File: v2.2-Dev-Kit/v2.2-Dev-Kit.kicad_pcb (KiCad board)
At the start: 2 copper layers, 42 x 59 mm, 30 parts, among them SW1 Up, SW2 Down, SW3 Left, SW4 Right, U1 WeMos D1 Mini

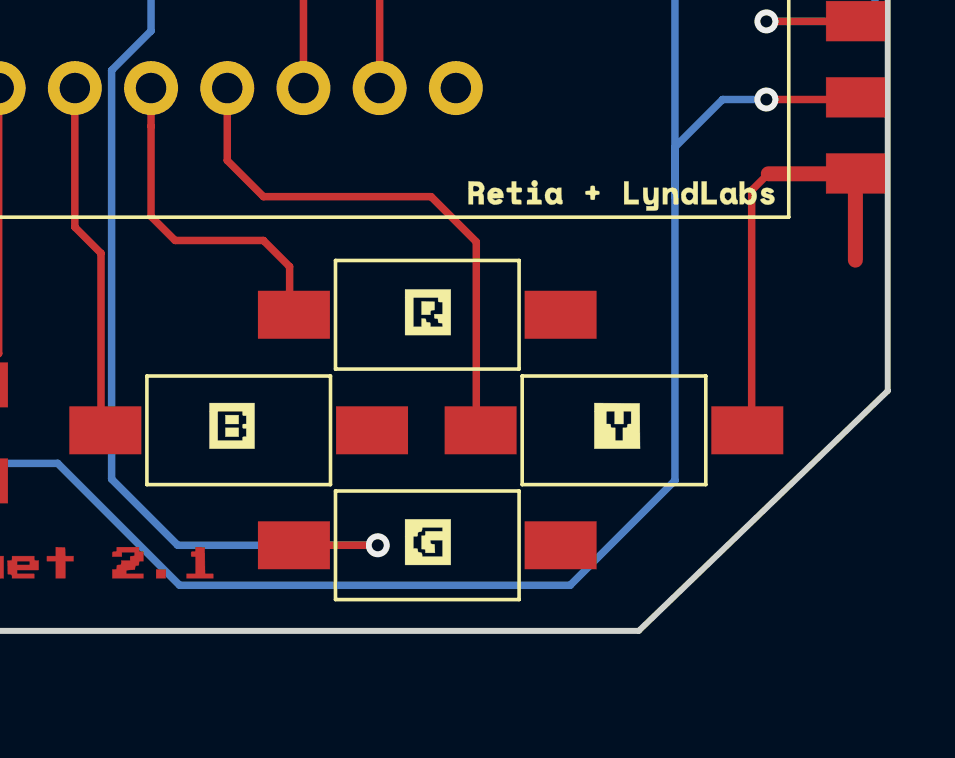
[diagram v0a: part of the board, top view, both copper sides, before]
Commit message: update v2.2 - delete old graphics
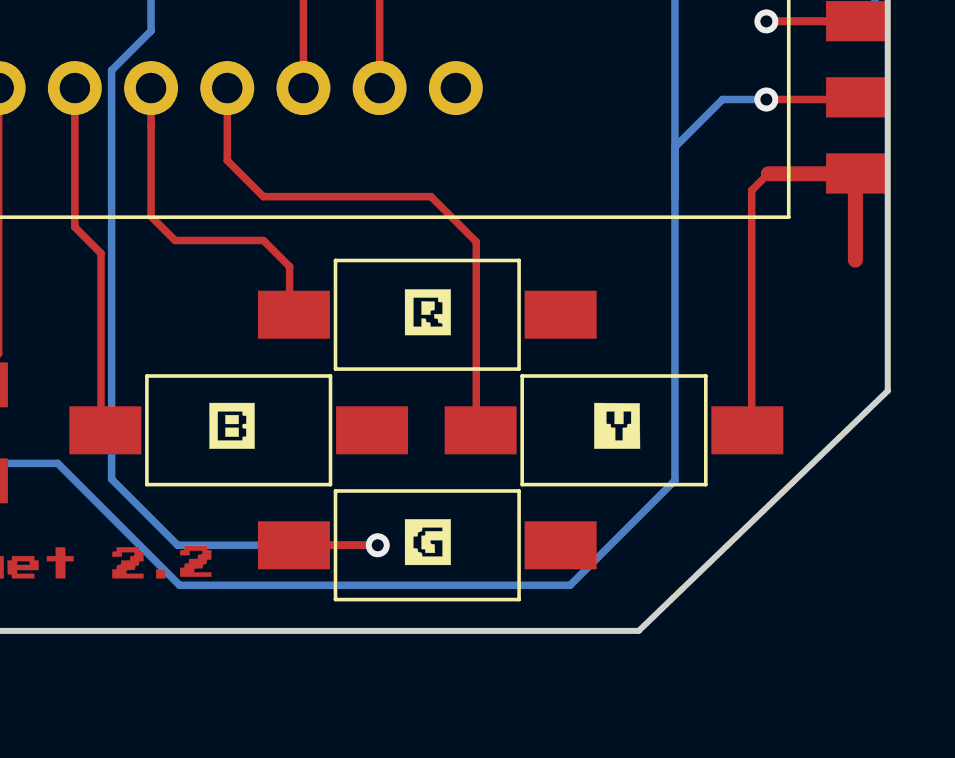
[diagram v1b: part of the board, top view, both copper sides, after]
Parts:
- removed the G*** at (0.00, 0.00) (x19)
- added G*** (x19): LOGO, LOGO, F.Cu at (0.00, 0.00)
- renumbered REF** to J1, Brd1 to U2
